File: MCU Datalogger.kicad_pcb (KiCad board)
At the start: 2 copper layers, 50.5 x 30.1 mm, 29 parts, among them J1 I2C, J2 ICSP, J3 Serial UART, J4 GPIO, U1 24LC1025, U2 24LC1025, U3 ATmega328P-A, U4 ds1337s+, Y1 32.768KHz, Y2 16 MHz

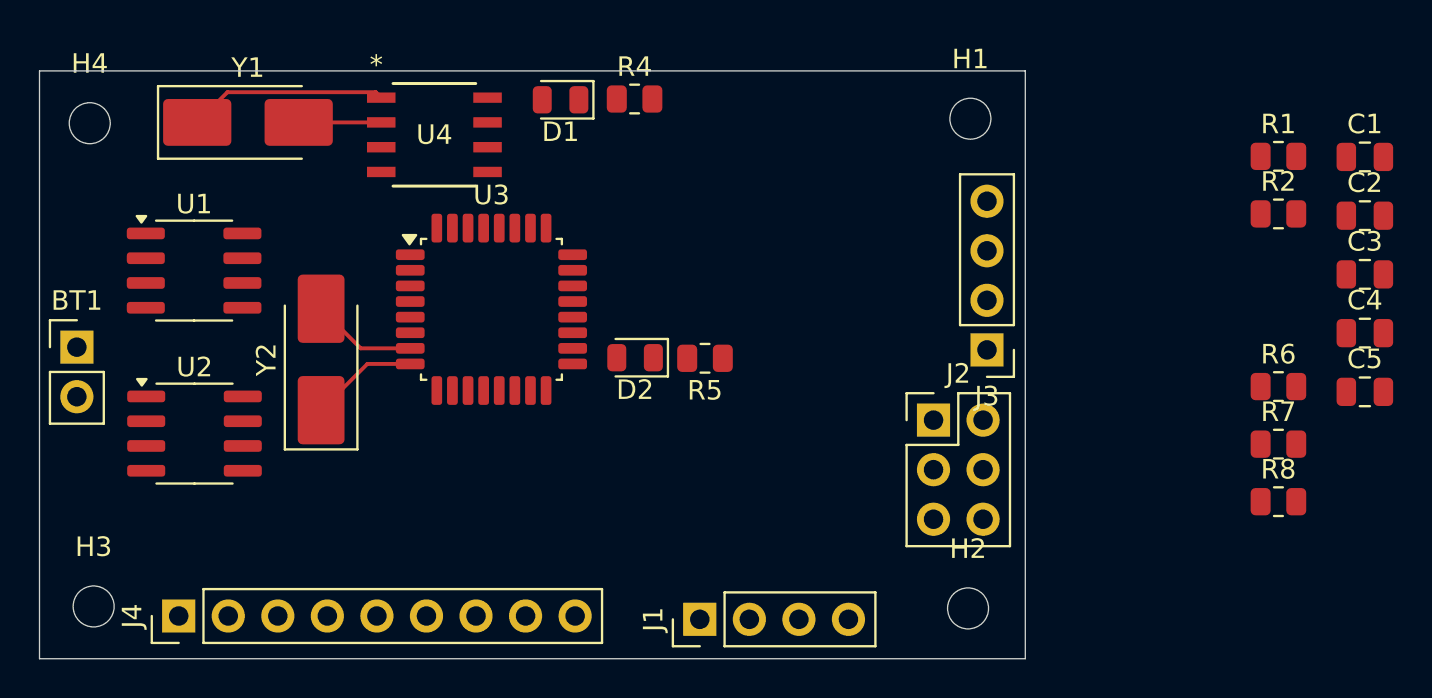
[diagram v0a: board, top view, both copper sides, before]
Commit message: done with routing
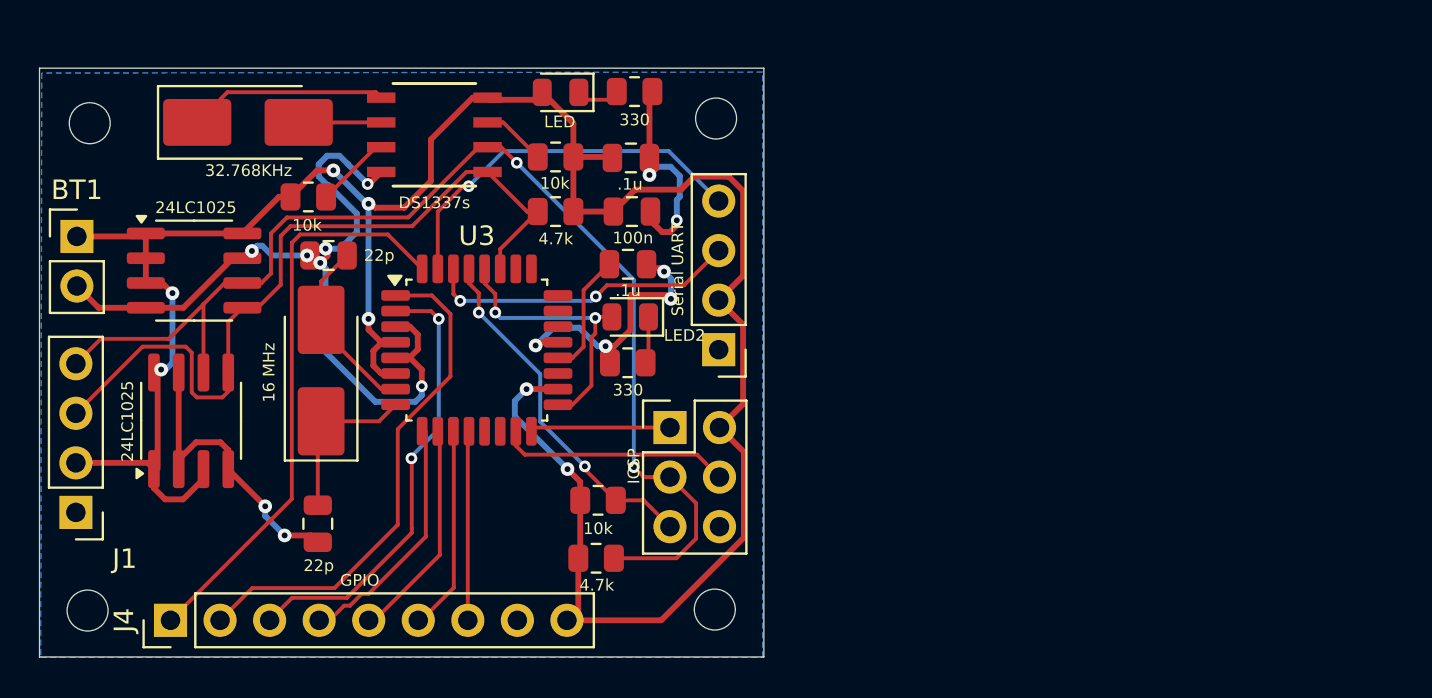
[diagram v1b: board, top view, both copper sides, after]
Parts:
- D2: value LED -> LED2
- moved C3 55.2 mm to (34.9, 72.8), turned to -90 degrees
- moved C2 53.2 mm to (35.5, 59.0), turned to 180 degrees
- moved R6 50.7 mm to (34.4, 56.0)
- moved R1 40.6 mm to (49.2, 74.5)
- moved R7 39.9 mm to (47.1, 54.0), turned to 180 degrees
- moved C5 38.7 mm to (51.0, 56.8)
- moved C4 37.9 mm to (50.8, 59.5)
- moved C1 37.6 mm to (51.0, 54.0)
- moved R2 37.1 mm to (47.1, 56.8), turned to 180 degrees
- moved R8 34.9 mm to (49.3, 71.5)
- moved J1 32.4 mm to (22.5, 72.2), turned to 180 degrees
- moved J3 13.8 mm to (55.5, 63.8)
- moved J2 13.5 mm to (53.0, 67.8)
- moved H1 13.0 mm to (55.3, 52.0)
- moved H2 13.0 mm to (55.2, 77.2)
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- renumbered U4 to DS1337s
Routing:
- net /VCC: track 0.00 -> 128.4 mm, vias 0 -> 7
- net GND: track 0.00 -> 85.7 mm, vias 0 -> 14
- net /SCL: track 0.00 -> 60.9 mm, vias 0 -> 2
- net /SDA: track 0.00 -> 40.3 mm
- net /D2: track 0.00 -> 29.5 mm
- net /D3: track 0.00 -> 26.3 mm
- net /D4: track 0.00 -> 23.2 mm, vias 0 -> 2
- net /TX: track 0.00 -> 20.4 mm, vias 0 -> 1
- net /RESET: track 0.00 -> 18.5 mm, vias 0 -> 2
- net /RX: track 0.00 -> 16.1 mm, vias 0 -> 2
- net /SCK: track 0.00 -> 14.4 mm, vias 0 -> 2
- net /D5: track 0.00 -> 12.6 mm
- net /MOSI: track 0.00 -> 11.8 mm
- net /D6: track 0.00 -> 11.4 mm
- net /D7: track 0.00 -> 10.5 mm
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- added copper zone on B.Cu, net GND
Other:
- board size 50.5 x 30.1 mm -> 37.1 x 30.2 mm

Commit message: done with 2layer
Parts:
- renumbered U3 to ATmega328P-A, J1 to I2C
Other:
- board text added: "GND"
- board text added: "MCU DataLogger with EEPROM. By: Nikunj Shah :>"
- board text added: "Version 1: 2-Layer PCB"
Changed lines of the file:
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@@
 		)
 		(property "Value" "22p"
-			(at -2.6 0 0)
+			(at -2.55 0 0)
 			(layer "F.SilkS")
 			(effects
@@
 		)
 		(property "Value" "10k"
-			(at -0.0625 1.45 0)
+			(at -0.0125 1.4 0)
 			(layer "F.SilkS")
 			(effects
@@
 		)
 		(property "Value" "LED2"
-			(at -2.7875 -0.95 180)
+			(at 2.3125 -0.1 270)
 			(layer "F.SilkS")
 			(effects
@@
 				(font
 					(size 0.6 0.6)
-					(thickness 0.075)
+					(thickness 0.12)
+					(bold yes)
 				)
 			)
@@
 		)
 		(property "Value" "24LC1025"
-			(at -0.025 -3.255 90)
+			(at -4.675 -0.005 180)
 			(layer "F.SilkS")
 			(effects
 				(font
 					(size 0.6 0.6)
-					(thickness 0.075)
+					(thickness 0.12)
+					(bold yes)
 				)
 			)
@@
 		(descr "TQFP, 32 Pin (JEDEC MS-026 variation ABA, https://www.jedec.org/document_search?search_api_views_fulltext=MS-026, https://ww1.microchip.com/downloads/en/PackagingSpec/00000049BZ.pdf#page=656), generated with kicad-footprint-generator ipc_gullwing_generator.py")
 		(tags "TQFP QFP")
-		(property "Reference" "U3"
-			(at 0 -5.85 0)
+		(property "Reference" "ATmega328P-A"
+			(at 0.15 5.9 0)
 			(layer "F.SilkS")
 			(effects
 				(font
-					(size 1 1)
-					(thickness 0.15)
+					(size 0.6 0.6)
+					(thickness 0.12)
+					(bold yes)
 				)
 			)
@@
 				(font
 					(size 0.6 0.6)
-					(thickness 0.075)
+					(thickness 0.12)
+					(bold yes)
 				)
 			)
@@
 		)
 		(property "Value" "ICSP"
-			(at -1.85 1.98 90)
+			(at -0.15 7.28 180)
 			(layer "F.SilkS")
 			(effects
 				(font
 					(size 0.6 0.6)
-					(thickness 0.075)
+					(thickness 0.12)
+					(bold yes)
 				)
 			)
@@
 				(font
 					(size 0.6 0.6)
-					(thickness 0.075)
+					(thickness 0.12)
+					(bold yes)
 				)
 			)
@@
 		(descr "Through hole straight pin header, 1x04, 2.54mm pitch, single row")
 		(tags "Through hole pin header THT 1x04 2.54mm single row")
-		(property "Reference" "J1"
-			(at -2.5 -2.38 0)
+		(property "Reference" "I2C"
+			(at 0 -2.28 0)
 			(layer "F.SilkS")
 			(effects
 				(font
-					(size 1 1)
-					(thickness 0.15)
+					(size 0.6 0.6)
+					(thickness 0.12)
+					(bold yes)
 				)
 			)
@@
 				(font
 					(size 0.6 0.6)
-					(thickness 0.075)
+					(thickness 0.12)
+					(bold yes)
 				)
 			)
@@
 		(layer "Edge.Cuts")
 	)
+	(gr_text "GND"
+		(at 24.4 73.25 0)
+		(layer "F.SilkS")
+		(effects
+			(font
+				(size 0.5 0.5)
+				(thickness 0.0625)
+			)
+			(justify left bottom)
+		)
+	)
+	(gr_text "GND"
+		(at 55.85 75.35 0)
+		(layer "F.SilkS")
+		(effects
+			(font
+				(size 0.5 0.5)
+				(thickness 0.0625)
+			)
+			(justify left bottom)
+		)
+	)
+	(gr_text "GND"
+		(at 21.75 62.75 0)
+		(layer "F.SilkS")
+		(effects
+			(font
+				(size 0.5 0.5)
+				(thickness 0.0625)
+			)
+			(justify left bottom)
+		)
+	)
+	(gr_text "GND"
+		(at 54.7 66 0)
+		(layer "F.SilkS")
+		(effects
+			(font
+				(size 0.5 0.5)
+				(thickness 0.0625)
+			)
+			(justify left bottom)
+		)
+	)
+	(gr_text "Version 1: 2-Layer PCB"
+		(at 47 75.6 0)
+		(layer "B.SilkS")
+		(effects
+			(font
+				(size 1 1)
+				(thickness 0.2)
+				(bold yes)
+			)
+			(justify left bottom mirror)
+		)
+	)
+	(gr_text "MCU DataLogger with EEPROM.\nBy: Nikunj Shah :>"
+		(at 50.95 54 0)
+		(layer "B.SilkS")
+		(effects
+			(font
+				(size 1 1)
+				(thickness 0.2)
+				(bold yes)
+			)
+			(justify left bottom mirror)
+		)
+	)
 	(segment

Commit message: done with rewiring
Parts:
- D2: value LED2 -> LED
- renumbered I2C to J1, ATmega328P-A to U3, DS1337s to U4
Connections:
- J2 pad 3: /SCL -> /SCK
- U3 pad 28: /SCK -> /SCL
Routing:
- net /SCL: track 60.9 -> 56.0 mm, vias 2 -> 4
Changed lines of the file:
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@@
 	(paper "A4")
 	(title_block
-		(date "2026-08-25")
-		(rev "1")
+		(date "2026-09-02")
+		(rev "2")
 		(comment 1 "2 layer PCB")
 	)
@@
 			)
 		)
-		(property "Value" "LED2"
+		(property "Value" "LED"
 			(at 2.3125 -0.1 270)
 			(layer "F.SilkS")
@@
 		(descr "TQFP, 32 Pin (JEDEC MS-026 variation ABA, https://www.jedec.org/document_search?search_api_views_fulltext=MS-026, https://ww1.microchip.com/downloads/en/PackagingSpec/00000049BZ.pdf#page=656), generated with kicad-footprint-generator ipc_gullwing_generator.py")
 		(tags "TQFP QFP")
-		(property "Reference" "ATmega328P-A"
+		(property "Reference" "U3"
 			(at 0.15 5.9 0)
 			(layer "F.SilkS")
@@
 			(layers "F.Cu" "F.Mask" "F.Paste")
 			(roundrect_rratio 0.25)
-			(net 8 "/SCK")
+			(net 9 "/SCL")
 			(pinfunction "PC5")
 			(pintype "bidirectional")
@@
 		(at 40.87585 52.815)
 		(tags "ds1337s+ ")
-		(property "Reference" "DS1337s"
+		(property "Reference" "U4"
 			(at 0 3.485 0)
 			(unlocked yes)
@@
 			(layers "*.Cu" "*.Mask")
 			(remove_unused_layers no)
-			(net 9 "/SCL")
+			(net 8 "/SCK")
 			(pinfunction "Pin_3")
 			(pintype "passive")
@@
 		(descr "Through hole straight pin header, 1x04, 2.54mm pitch, single row")
 		(tags "Through hole pin header THT 1x04 2.54mm single row")
-		(property "Reference" "I2C"
+		(property "Reference" "J1"
 			(at 0 -2.28 0)
 			(layer "F.SilkS")
@@
 	)
 	(segment
-		(start 43.45 60.424999)
-		(end 43.45 59.6875)
-		(width 0.2)
-		(layer "F.Cu")
-		(net 8)
-	)
-	(segment
-		(start 43.998527 61.926)
-		(end 43.998527 60.973526)
-		(width 0.2)
-		(layer "F.Cu")
-		(net 8)
-	)
-	(segment
-		(start 49.975 62.15)
-		(end 49.1735 62.15)
-		(width 0.2)
-		(layer "F.Cu")
-		(net 8)
-	)
-	(segment
-		(start 49.05 62.2)
-		(end 49.1235 62.2)
+		(start 47.148494 66.714006)
+		(end 47.2125 66.65)
 		(width 0.2)
 		(layer "F.Cu")
@@
 	)
 	(segment
-		(start 49.1235 62.2)
-		(end 49.1235 63.0015)
+		(start 52.95 70.36)
+		(end 50.001 70.36)
 		(width 0.2)
 		(layer "F.Cu")
@@
 	)
 	(segment
-		(start 48.9245 65.675499)
-		(end 47.949999 66.65)
+		(start 47.148494 67.22)
+		(end 47.148494 66.714006)
 		(width 0.2)
 		(layer "F.Cu")
@@
 	)
 	(segment
-		(start 49.1735 62.15)
-		(end 49.1235 62.2)
+		(start 47.844654 66.65)
+		(end 47.2125 66.65)
 		(width 0.2)
 		(layer "F.Cu")
@@
 	)
 	(segment
-		(start 47.949999 66.65)
-		(end 47.2125 66.65)
+		(start 50.001 70.36)
+		(end 49.45 69.809)
 		(width 0.2)
 		(layer "F.Cu")
@@
 	)
 	(segment
-		(start 43.998527 60.973526)
-		(end 43.45 60.424999)
+		(start 49.975 62.15)
+		(end 48.949 63.176)
 		(width 0.2)
 		(layer "F.Cu")
@@
 	)
 	(segment
-		(start 49.1235 63.0015)
-		(end 48.9245 63.2005)
+		(start 48.949 65.545654)
+		(end 47.844654 66.65)
 		(width 0.2)
 		(layer "F.Cu")
@@
 	)
 	(segment
-		(start 48.9245 63.2005)
-		(end 48.9245 65.675499)
+		(start 48.949 63.176)
+		(end 48.949 65.545654)
 		(width 0.2)
 		(layer "F.Cu")
@@
 	)
 	(via
-		(at 43.998527 61.926)
+		(at 47.148494 67.22)
 		(size 0.6)
 		(drill 0.3)
@@
 	)
 	(via
-		(at 49.1235 62.2)
+		(at 49.45 69.809)
 		(size 0.6)
 		(drill 0.3)
@@
 	)
 	(segment
-		(start 43.976 61.926)
-		(end 43.998527 61.926)
+		(start 47.148494 67.507494)
+		(end 47.148494 67.22)
 		(width 0.2)
 		(layer "B.Cu")
@@
 	)
 	(segment
-		(start 44.25 62.2)
-		(end 43.976 61.926)
+		(start 49.45 69.809)
+		(end 47.148494 67.507494)
 		(width 0.2)
 		(layer "B.Cu")
@@
 	)
 	(segment
-		(start 49.1235 62.2)
-		(end 44.25 62.2)
-		(width 0.2)
-		(layer "B.Cu")
-		(net 8)
-	)
-	(segment
-		(start 51.61 70.36)
-		(end 51.1 69.85)
-		(width 0.2)
-		(layer "F.Cu")
-		(net 9)
-	)
-	(segment
-		(start 54.289 71.699)
-		(end 52.95 70.36)
-		(width 0.2)
-		(layer "F.Cu")
-		(net 9)
-	)
-	(segment
-		(start 50.0775 74.52)
-		(end 53.28 74.52)
-		(width 0.2)
-		(layer "F.Cu")
-		(net 9)
-	)
-	(segment
 		(start 33.31713 57.051)
 		(end 39.53545 57.051)
@@
 	)
 	(segment
-		(start 43.13645 53.45)
-		(end 43.6 53.45)
+		(start 43.45 58.62647)
+		(end 45.05397 57.0225)
 		(width 0.2)
 		(layer "F.Cu")
@@
 	)
 	(segment
-		(start 51.1 69.85)
-		(end 51.141 69.809)
+		(start 43.13645 53.45)
+		(end 43.6 53.45)
 		(width 0.2)
 		(layer "F.Cu")
@@
 	)
 	(segment
-		(start 45.1 54.25)
-		(end 44.3 53.45)
+		(start 43.45 59.6875)
+		(end 43.45 58.62647)
 		(width 0.2)
 		(layer "F.Cu")
@@
 	)
 	(segment
-		(start 52.95 70.36)
-		(end 51.61 70.36)
+		(start 27.267 63.273)
+		(end 29.04 61.5)
 		(width 0.2)
 		(layer "F.Cu")
@@
 	)
 	(segment
-		(start 27.267 63.273)
-		(end 29.04 61.5)
+		(start 50.0775 74.0775)
+		(end 49.05 73.05)
 		(width 0.2)
 		(layer "F.Cu")
@@
 	)
 	(segment
-		(start 54.289 73.511)
-		(end 54.289 71.699)
+		(start 44.15 53.45)
+		(end 43.6 53.45)
 		(width 0.2)
 		(layer "F.Cu")
@@
 	)
 	(segment
-		(start 44.3 53.45)
-		(end 43.6 53.45)
+		(start 43.45 60.424999)
+		(end 43.45 59.6875)
+		(width 0.2)
+		(layer "F.Cu")
+		(net 9)
+	)
+	(segment
+		(start 45.05 54.35)
+		(end 44.15 53.45)
 		(width 0.2)
 		(layer "F.Cu")
@@
 	)
 	(segment
+		(start 43.751 63.299)
+		(end 43.751 60.725999)
+		(width 0.2)
+		(layer "F.Cu")
+		(net 9)
+	)
+	(segment
 		(start 23.777 63.273)
 		(end 27.267 63.273)
@@
 	)
 	(segment
-		(start 53.28 74.52)
-		(end 54.289 73.511)
+		(start 43.712735 63.337265)
+		(end 43.751 63.299)
+		(width 0.2)
+		(layer "F.Cu")
+		(net 9)
+	)
+	(segment
+		(start 50.0775 74.52)
+		(end 50.0775 74.0775)
+		(width 0.2)
+		(layer "F.Cu")
+		(net 9)
+	)
+	(segment
+		(start 43.751 60.725999)
+		(end 43.45 60.424999)
 		(width 0.2)
 		(layer "F.Cu")
@@
 	)
 	(via
-		(at 51.1 69.85)
+		(at 43.712735 63.337265)
+		(size 0.6)
+		(drill 0.3)
+		(layers "F.Cu" "B.Cu")
+		(net 9)
+	)
+	(via
+		(at 45.05397 57.0225)
 		(size 0.6)
 		(drill 0.3)
@@
 	)
 	(via
-		(at 45.1 54.25)
+		(at 45.05 54.35)
+		(size 0.6)
+		(drill 0.3)
+		(layers "F.Cu" "B.Cu")
+		(net 9)
+	)
+	(via
+		(at 49.05 73.05)
 		(size 0.6)
 		(drill 0.3)
@@
 	)
 	(segment
-		(start 51.1 69.85)
-		(end 51.1 60.25)
+		(start 45.05 57.01853)
+		(end 45.05 54.35)
 		(width 0.2)
 		(layer "B.Cu")
@@
 	)
 	(segment
-		(start 51.1 60.25)
-		(end 45.1 54.25)
+		(start 49.05 73.05)
+		(end 43.712735 67.712735)
+		(width 0.2)
+		(layer "B.Cu")
+		(net 9)
+	)
+	(segment
+		(start 45.05397 57.0225)
+		(end 45.05 57.01853)
+		(width 0.2)
+		(layer "B.Cu")
+		(net 9)
+	)
+	(segment
+		(start 43.712735 67.712735)
+		(end 43.712735 63.337265)
 		(width 0.2)
 		(layer "B.Cu")
@@
 	)
 	(segment
-		(start 45.6425 56.7625)
-		(end 43.6 54.72)
+		(start 43.6 54.72)
+		(end 45.63 56.75)
 		(width 0.2)
 		(layer "F.Cu")
@@
 	)
 	(segment
-		(start 46.175 56.75)
-		(end 46.1625 56.7625)
+		(start 45.63 56.75)
+		(end 46.175 56.75)
 		(width 0.2)
 		(layer "F.Cu")
@@
 	)
 	(segment
-		(start 46.1625 56.7625)
-		(end 45.6425 56.7625)
+		(start 46.175 56.75)
+		(end 46.1625 56.7625)
 		(width 0.2)
 		(layer "F.Cu")
